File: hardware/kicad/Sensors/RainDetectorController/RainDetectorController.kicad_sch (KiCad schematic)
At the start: 15 parts, among them J1 Conn_01x04_Socket, J2 Conn_01x04_Socket, J3 HEATER_CTRL, J4 RAIN_SIGNAL, Q1 AO3400A, U1 ICM7555xB

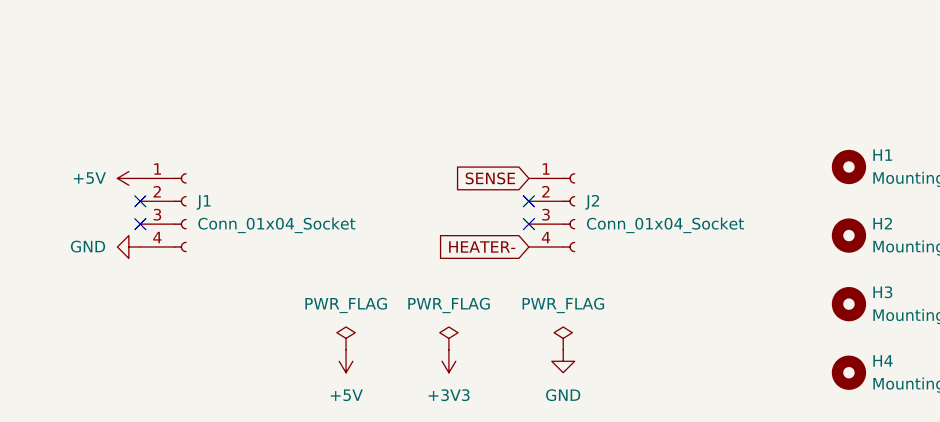
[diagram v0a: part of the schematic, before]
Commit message: Update RainDetector board connectors, outlines and parts kits
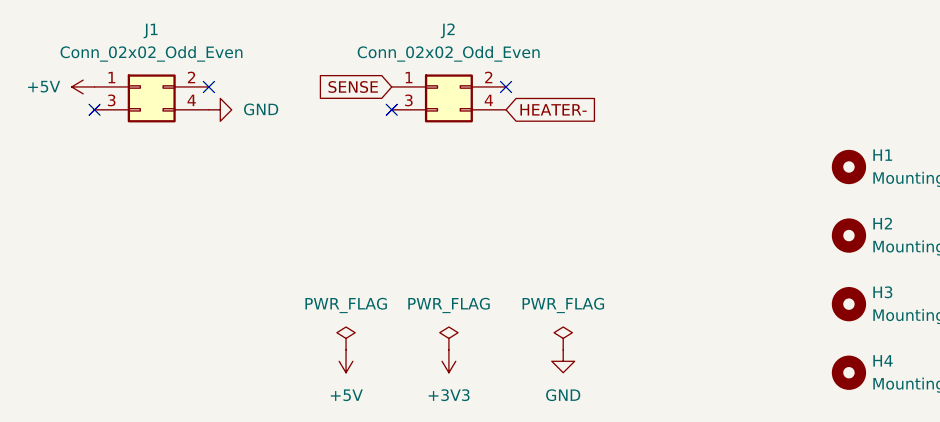
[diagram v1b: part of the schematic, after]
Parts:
- removed J1, J2: Conn_01x04_Socket, Connector_PinSocket_2.54mm:PinSocket_1x04_P2.54mm_Vertical, symbol Connector:Conn_01x04_Socket
- added J1, J2: Conn_02x02_Odd_Even, Connector_PinSocket_2.54mm:PinSocket_2x02_P2.54mm_Vertical, symbol Connector_Generic:Conn_02x02_Odd_Even
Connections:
- net +5V: now also J1.1 (Pin_1)
- net GND: now also J1.4 (Pin_4)
- net HEATER-: now also J2.4 (Pin_4)
- net SENSE: now also J2.1 (Pin_1)
